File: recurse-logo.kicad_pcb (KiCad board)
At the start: 2 copper layers, 60 x 75 mm, 18 parts, among them Q1 MMBT3904, Q2 MMBT3904

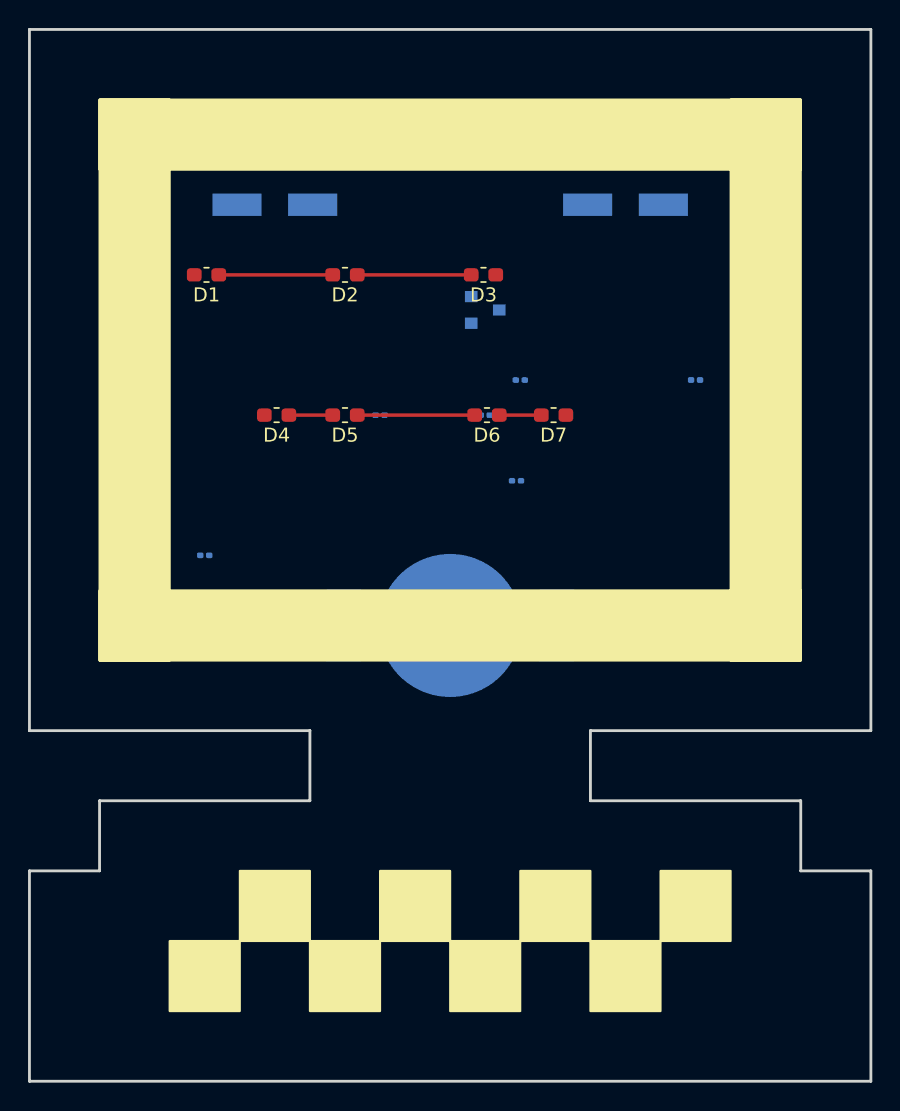
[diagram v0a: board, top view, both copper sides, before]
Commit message: Updates and change to relative paths
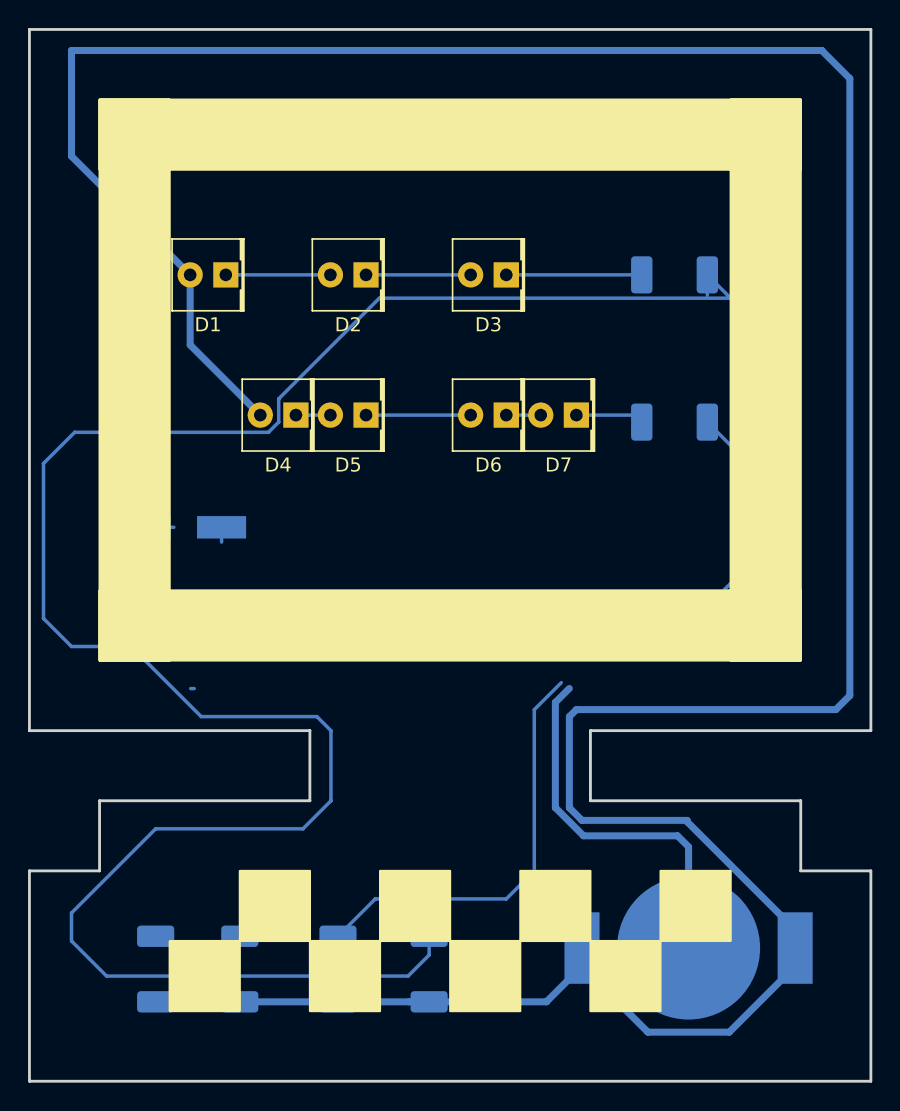
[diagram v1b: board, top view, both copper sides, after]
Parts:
- D1, D2, D3, D4, D5, D6, D7: footprint Inductor_SMD:L_0603_1608Metric_Pad1.05x0.95mm_HandSolder -> LED_THT:LED_Rectangular_W5.0mm_H5.0mm
- R1, R2, R3, R4, R5, R6: footprint Resistor_SMD:R_0201_0603Metric -> Resistor_SMD:R_2010_5025Metric_Pad1.52x2.65mm_HandSolder
- moved Q1 43.0 mm to (59.0, 55.5)
- moved R4 42.6 mm to (21.0, 79.0), turned to 90 degrees
- moved R2 42.5 mm to (40.5, 79.0), turned to 270 degrees
- moved C2 39.0 mm to (23.0, 47.5), turned to 180 degrees
- moved R3 37.1 mm to (34.0, 79.0), turned to 270 degrees
- moved C1 32.2 mm to (23.0, 56.0), turned to 180 degrees
- moved R5 29.6 mm to (27.0, 79.0), turned to 90 degrees
- moved BT1 28.6 mm to (59.0, 77.5)
- moved Q2 24.0 mm to (49.5, 55.5), turned to 270 degrees
- moved R6 13.5 mm to (58.0, 40.0)
- moved R1 7.65 mm to (58.0, 29.5), turned to 180 degrees
- moved D3 1.62 mm to (46.0, 29.5)
- moved D7 1.62 mm to (51.0, 39.5)
- moved D2 1.50 mm to (36.0, 29.5)
- moved D5 1.50 mm to (36.0, 39.5)
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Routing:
- net VCC: track 0.00 -> 233.2 mm
- net Net-(C1-Pad2): track 0.00 -> 182.4 mm
- net Net-(C2-Pad1): track 0.00 -> 32.6 mm
- net Net-(C2-Pad2): track 0.00 -> 29.7 mm
- net GND: track 0.00 -> 29.6 mm
- net Net-(D3-Pad1): track 0.00 -> 9.66 mm
- net Net-(D7-Pad1): track 0.00 -> 4.87 mm
- net Net-(C1-Pad1): track 0.00 -> 2.25 mm
- net Net-(D5-Pad1): track 8.38 -> 7.46 mm
- net Net-(D4-Pad1): track 3.12 -> 2.46 mm
- net Net-(D2-Pad1): track 8.12 -> 7.46 mm
- net Net-(D1-Pad1): track 8.12 -> 7.46 mm
- net Net-(D6-Pad1): track 3.00 -> 2.46 mm

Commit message: Wired it up! needs finishing touches
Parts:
- moved R4 42.6 mm to (52.0, 49.7), turned to 270 degrees
- moved C1 40.1 mm to (63.0, 54.3), turned to 270 degrees
- moved R5 31.7 mm to (39.1, 49.7)
- moved R2 29.7 mm to (45.5, 49.7)
- moved R3 29.5 mm to (32.2, 49.6), turned to 90 degrees
- moved BT1 16.9 mm to (42.4, 74.3), turned to 90 degrees
- moved Q2 16.5 mm to (33.0, 57.1), turned to 180 degrees
- moved Q1 8.82 mm to (50.3, 57.1)
- moved C2 6.90 mm to (21.6, 54.3), turned to 270 degrees
- moved R6 1.29 mm to (56.8, 39.5)
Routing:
- net GND: track 29.6 -> 206.8 mm
- net Net-(C1-Pad2): track 182.4 -> 62.2 mm
- net Net-(C2-Pad1): track 32.6 -> 142.9 mm
- net Net-(C1-Pad1): track 2.25 -> 60.2 mm
- net VCC: track 233.2 -> 184.6 mm
- net Net-(C2-Pad2): track 29.7 -> 54.1 mm
- net Net-(D7-Pad1): track 4.87 -> 3.47 mm
- net Net-(D3-Pad1): track 9.66 -> 10.8 mm
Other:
- net class VCC added: clearance 0.2, trace_width 0.5, via_dia 0.8, via_drill 0.4

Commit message: Finished\!
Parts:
- C2: value 100mF -> 100uF
- moved D7 0.20 mm to (51.2, 39.5)
- moved D4 0.20 mm to (30.8, 39.5)
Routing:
- net VCC: track 184.6 -> 183.1 mm
- net Net-(C2-Pad1): track 142.9 -> 144.2 mm
- net Net-(C2-Pad2): track 54.1 -> 54.8 mm
- added copper zone on B.Cu, net GND
- added copper zone on F.Cu, net GND
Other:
- board size 60 x 75 mm -> 60 x 83 mm
